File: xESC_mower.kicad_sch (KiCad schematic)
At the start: 48 parts, among them J25 Conn_01x05, J34 Screw_Terminal_01x03, J37 Conn_02x03_Odd_Even, J40 Screw_Terminal_01x02, J43 Conn_01x02, J49 10127820-1022LF, U19 2.54mm 2x2 socket, U22 2.54mm 2x2 socket, U25 2.54mm 2x2 socket, U29 LV2862XDDC, U31 2.54mm 1x6 socket, U34 2.54mm 1x6 socket, U37 2.54mm 1x9 socket, U40 2.54mm 1x5 socket, U9 xESC2

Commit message: Routing progress and vertical USB
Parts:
- J49: Digikey PN (none) -> 609-4876-ND
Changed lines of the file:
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@@
+			)
+		)
+		(property "Digikey PN" "609-4876-ND"
+			(at 240.03 161.29 0)
+			(effects
+				(font
+					(size 1.27 1.27)
+				)
+				(hide yes)
 			)
 		)

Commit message: Incremental routing updates
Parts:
- removed J25: Conn_01x05, Connector_JST:JST_XH_B5B-XH-A_1x05_P2.50mm_Vertical, symbol Connector_Generic:Conn_01x05
- removed J40: Screw_Terminal_01x02, TerminalBlock_Phoenix:TerminalBlock_Phoenix_MKDS-1,5-2-5.08_1x02_P5.08mm_Horizontal, symbol Connector:Screw_Terminal_01x02
- removed J43: Conn_01x02, Connector_AMASS:AMASS_XT30U-M_1x02_P5.0mm_Vertical, symbol Connector_Generic:Conn_01x02

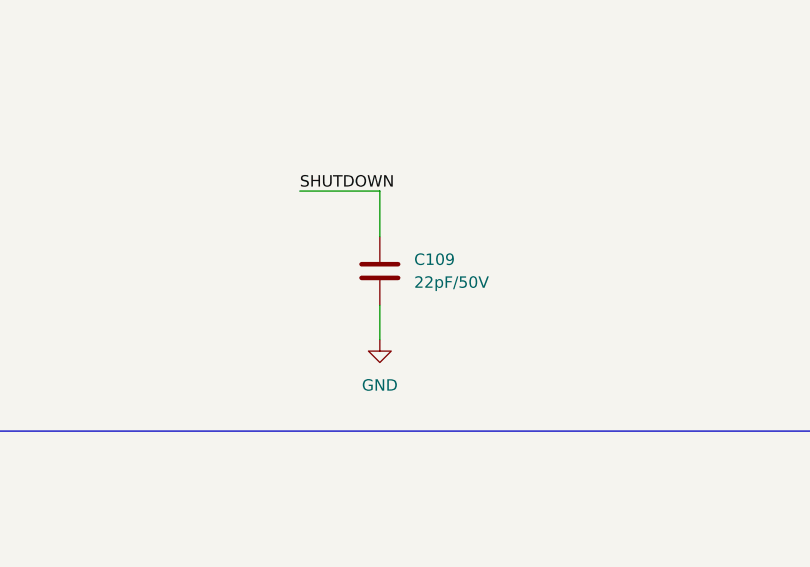
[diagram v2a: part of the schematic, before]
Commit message: Additional routing
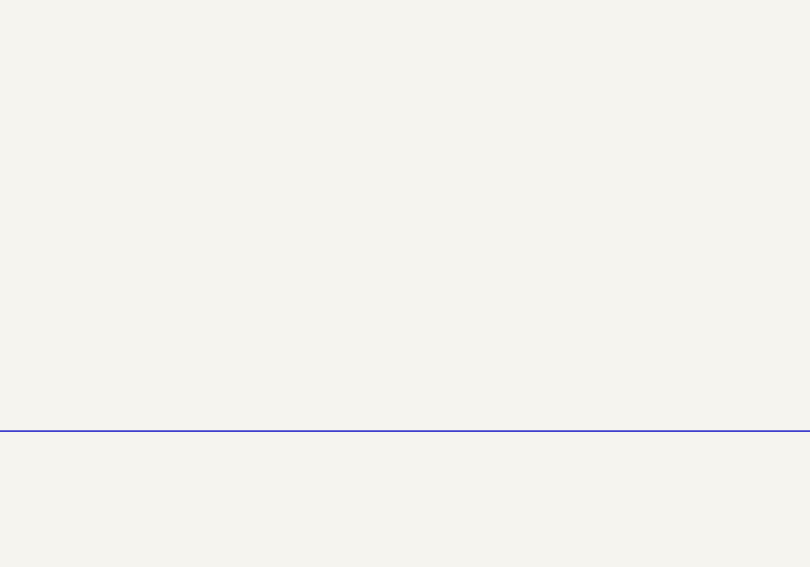
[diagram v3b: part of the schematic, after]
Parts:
- removed C109: 22pF/50V, Capacitor_SMD:C_0603_1608Metric, symbol Device:C

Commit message: Routing progress
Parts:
- D24: now not fitted
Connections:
- net 5V is gone; now on net 5V_Main: C102.1, C103.1, D24.1 (K), D32.2 (A), J37.1 (Pin_1), L6.2, R28.1, U9.5V
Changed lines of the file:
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@@
+	)
+	(junction
+		(at 64.77 60.96)
+		(diameter 0)
+		(color 0 0 0 0)
 	)
 	(junction
@@
 	(junction
 		(at 69.85 100.33)
+		(diameter 0)
+		(color 0 0 0 0)
+	)
+	(junction
+		(at 57.15 60.96)
 		(diameter 0)
 		(color 0 0 0 0)
@@
 	(wire
 		(pts
+			(xy 64.77 57.15) (xy 64.77 60.96)
+		)
+		(stroke
+			(width 0)
+			(type default)
+		)
+	)
+	(wire
+		(pts
 			(xy 124.46 30.48) (xy 118.11 30.48)
 		)
@@
 		(pts
 			(xy 213.36 106.68) (xy 222.25 106.68)
+		)
+		(stroke
+			(width 0)
+			(type default)
+		)
+	)
+	(wire
+		(pts
+			(xy 57.15 60.96) (xy 57.15 57.15)
+		)
+		(stroke
+			(width 0)
+			(type default)
+		)
+	)
+	(wire
+		(pts
+			(xy 57.15 57.15) (xy 64.77 57.15)
 		)
 		(stroke
@@
 		(in_bom yes)
 		(on_board yes)
-		(dnp no)
+		(dnp yes)
 		(fields_autoplaced yes)
 		(property "Reference" "D24"

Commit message: Further routing progress
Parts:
- removed J34: Screw_Terminal_01x03, TerminalBlock_Phoenix:TerminalBlock_Phoenix_MKDS-1,5-3-5.08_1x03_P5.08mm_Horizontal, symbol Connector:Screw_Terminal_01x03
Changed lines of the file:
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@@
 	)
 	(junction
+		(at 222.25 106.68)
+		(diameter 0)
+		(color 0 0 0 0)
+	)
+	(junction
 		(at 44.45 100.33)
 		(diameter 0)
@@
 	)
 	(junction
+		(at 214.63 99.06)
+		(diameter 0)
+		(color 0 0 0 0)
+	)
+	(junction
 		(at 167.64 46.99)
 		(diameter 0)
@@
 	)
 	(junction
-		(at 214.63 99.06)
-		(diameter 0)
-		(color 0 0 0 0)
-	)
-	(junction
 		(at 54.61 107.95)
 		(diameter 0)
@@
 	)
 	(junction
-		(at 184.15 46.99)
+		(at 205.74 102.87)
 		(diameter 0)
 		(color 0 0 0 0)
 	)
 	(junction
-		(at 44.45 107.95)
+		(at 184.15 46.99)
 		(diameter 0)
 		(color 0 0 0 0)
 	)
 	(junction
-		(at 49.53 107.95)
+		(at 44.45 107.95)
 		(diameter 0)
 		(color 0 0 0 0)
 	)
 	(junction
-		(at 205.74 102.87)
+		(at 49.53 107.95)
 		(diameter 0)
 		(color 0 0 0 0)
@@
 	)
 	(junction
-		(at 222.25 106.68)
-		(diameter 0)
-		(color 0 0 0 0)
-	)
-	(junction
 		(at 78.74 36.83)
 		(diameter 0)
@@
 	(wire
 		(pts
+			(xy 214.63 99.06) (xy 226.06 99.06)
+		)
+		(stroke
+			(width 0)
+			(type default)
+		)
+	)
+	(wire
+		(pts
 			(xy 205.74 102.87) (xy 205.74 113.03)
 		)
@@
 	(wire
 		(pts
-			(xy 242.57 99.06) (xy 242.57 100.33)
-		)
-		(stroke
-			(width 0)
-			(type default)
-		)
-	)
-	(wire
-		(pts
 			(xy 284.48 121.92) (xy 306.07 121.92)
 		)
@@
 	(wire
 		(pts
-			(xy 214.63 99.06) (xy 242.57 99.06)
+			(xy 254 121.92) (xy 271.78 121.92)
 		)
 		(stroke
@@
 	(wire
 		(pts
-			(xy 254 121.92) (xy 271.78 121.92)
+			(xy 118.11 41.91) (xy 132.08 41.91)
 		)
 		(stroke
@@
 	(wire
 		(pts
-			(xy 118.11 41.91) (xy 132.08 41.91)
+			(xy 69.85 107.95) (xy 74.93 107.95)
 		)
 		(stroke
@@
 	(wire
 		(pts
-			(xy 69.85 107.95) (xy 74.93 107.95)
+			(xy 195.58 99.06) (xy 214.63 99.06)
 		)
 		(stroke
@@
 	(wire
 		(pts
-			(xy 195.58 99.06) (xy 214.63 99.06)
+			(xy 132.08 104.14) (xy 142.24 104.14)
 		)
 		(stroke
@@
 	(wire
 		(pts
-			(xy 132.08 104.14) (xy 142.24 104.14)
+			(xy 222.25 106.68) (xy 226.06 106.68)
 		)
 		(stroke
@@
 	(wire
 		(pts
-			(xy 222.25 106.68) (xy 242.57 106.68)
-		)
-		(stroke
-			(width 0)
-			(type default)
-		)
-	)
-	(wire
-		(pts
 			(xy 29.21 100.33) (xy 39.37 100.33)
 		)
@@
 	(wire
 		(pts
-			(xy 242.57 106.68) (xy 242.57 105.41)
-		)
-		(stroke
-			(width 0)
-			(type default)
-		)
-	)
-	(wire
-		(pts
 			(xy 74.93 100.33) (xy 90.17 100.33)
 		)
@@
 	(wire
 		(pts
-			(xy 57.15 57.15) (xy 64.77 57.15)
+			(xy 205.74 102.87) (xy 226.06 102.87)
 		)
 		(stroke
@@
 	(wire
 		(pts
-			(xy 193.04 121.92) (xy 243.84 121.92)
+			(xy 57.15 57.15) (xy 64.77 57.15)
 		)
 		(stroke
@@
 	(wire
 		(pts
-			(xy 222.25 149.86) (xy 227.33 149.86)
+			(xy 193.04 121.92) (xy 243.84 121.92)
 		)
 		(stroke
@@
 	(wire
 		(pts
-			(xy 205.74 102.87) (xy 242.57 102.87)
+			(xy 222.25 149.86) (xy 227.33 149.86)
 		)
 		(stroke
@@
 					(unit 1)
 				)
-			)
-		)
-	)
-	(symbol
-		(lib_id "Connector:Screw_Terminal_01x03")
-		(at 247.65 102.87 0)
-		(unit 1)
-		(exclude_from_sim no)
-		(in_bom yes)
-		(on_board yes)
-		(dnp no)
-		(fields_autoplaced yes)
-		(property "Reference" "J34"
-			(at 250.19 101.5999 0)
-			(effects
-				(font
-					(size 1.27 1.27)
-				)
-				(justify left)
-			)
-		)
-		(property "Value" "Screw_Terminal_01x03"
-			(at 250.19 104.1399 0)
-			(effects
-				(font
-					(size 1.27 1.27)
-				)
-				(justify left)
-			)
-		)
-		(property "Footprint" "TerminalBlock_Phoenix:TerminalBlock_Phoenix_MKDS-1,5-3-5.08_1x03_P5.08mm_Horizontal"
-			(at 247.65 102.87 0)
-			(effects
-				(font
-					(size 1.27 1.27)
-				)
-				(hide yes)
-			)
-		)
-		(property "Datasheet" "~"
-			(at 247.65 102.87 0)
-			(effects
-				(font
-					(size 1.27 1.27)
-				)
-				(hide yes)
-			)
-		)
-		(property "Description" "Generic screw terminal, single row, 01x03, script generated (kicad-library-utils/schlib/autogen/connector/)"
-			(at 247.65 102.87 0)
-			(effects
-				(font
-					(size 1.27 1.27)
-				)
-				(hide yes)
-			)
-		)
-		(property "Field4" ""
-			(at 247.65 102.87 0)
-			(effects
-				(font
-					(size 1.27 1.27)
-				)
-				(hide yes)
-			)
-		)
-		(property "Field5" ""
-			(at 247.65 102.87 0)
-			(effects
-				(font
-					(size 1.27 1.27)
-				)
-				(hide yes)
-			)
-		)
-		(property "Field6" ""
-			(at 247.65 102.87 0)
-			(effects
-				(font
-					(size 1.27 1.27)
-				)
-				(hide yes)
-			)
-		)
-		(property "Field7" ""
-			(at 247.65 102.87 0)
-			(effects
-				(font
-					(size 1.27 1.27)
-				)
-				(hide yes)
-			)
-		)
-		(property "JLC" "C557666"
-			(at 247.65 102.87 0)
-			(effects
-				(font
-					(size 1.27 1.27)
-				)
-				(hide yes)
-			)
-		)
-		(property "Part Description" ""
-			(at 247.65 102.87 0)
-			(effects
-				(font
-					(size 1.27 1.27)
-				)
-				(hide yes)
-			)
-		)
-		(property "Height" ""
-			(at 247.65 102.87 0)
-			(effects
-				(font
-					(size 1.27 1.27)
-				)
-				(hide yes)
-			)
-		)
-		(property "Manufacturer_Name" ""
-			(at 247.65 102.87 0)
-			(effects
-				(font
-					(size 1.27 1.27)
-				)
-				(hide yes)
-			)
-		)
-		(property "Manufacturer_Part_Number" ""
-			(at 247.65 102.87 0)
-			(effects
-				(font
-					(size 1.27 1.27)
-				)
-				(hide yes)
-			)
-		)
-		(property "Mouser Part Number" ""
-			(at 247.65 102.87 0)
-			(effects
-				(font
-					(size 1.27 1.27)
-				)
-				(hide yes)
-			)
-		)
-		(property "Mouser Price/Stock" ""
-			(at 247.65 102.87 0)
-			(effects
-				(font
-					(size 1.27 1.27)
-				)
-				(hide yes)
-			)
-		)
-		(pin "3"
-		)
-		(pin "2"
-		)
-		(pin "1"
-		)
-		(instances
-			(project "hw-openmower-universal"
-				(path "/e12e8a63-1d1b-4736-9aba-a87a258b2b11/35c1a146-5cd7-4cc8-a12d-17de73f02598"
-					(reference "J34")
-					(unit 1)
-				)

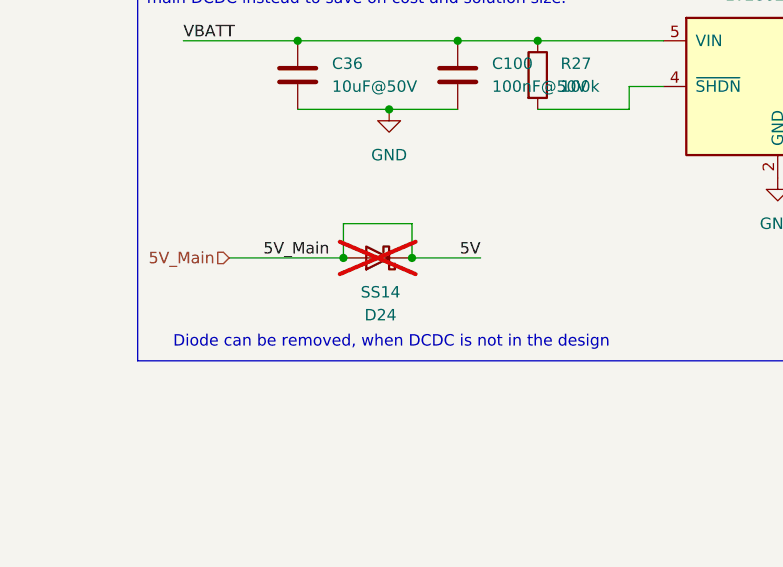
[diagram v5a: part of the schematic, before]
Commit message: Review ready layout
DRC mostly clean.  Need to add GND via stitching and GND return vias yet, and general review
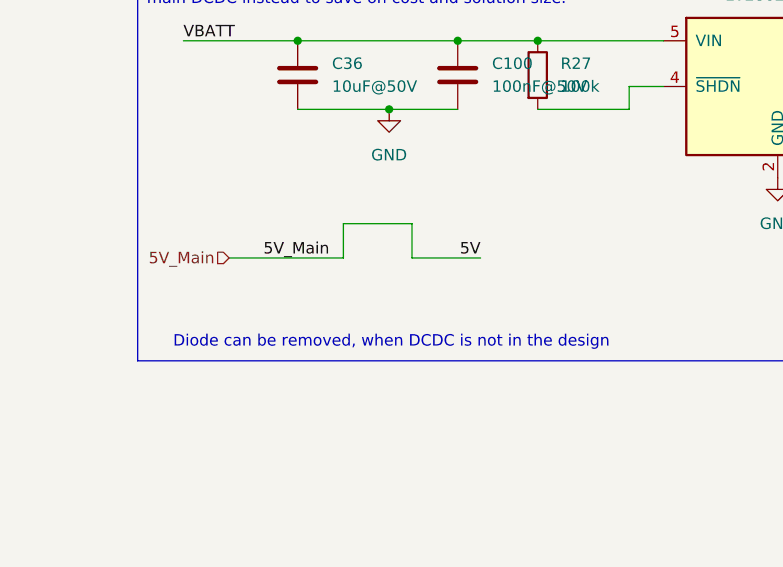
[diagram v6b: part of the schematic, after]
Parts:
- removed D24: SS14, Diode_SMD:D_SMA, symbol Diode:SS14
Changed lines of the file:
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@@
-	)
-	(junction
-		(at 64.77 60.96)
-		(diameter 0)
-		(color 0 0 0 0)
 	)
 	(junction
@@
 	(junction
 		(at 69.85 100.33)
-		(diameter 0)
-		(color 0 0 0 0)
-	)
-	(junction
-		(at 57.15 60.96)
 		(diameter 0)
 		(color 0 0 0 0)
@@
 					(unit 1)
 				)
-			)
-		)
-	)
-	(symbol
-		(lib_id "Diode:SS14")
-		(at 60.96 60.96 180)
-		(unit 1)
-		(exclude_from_sim no)
-		(in_bom yes)
-		(on_board yes)
-		(dnp yes)
-		(fields_autoplaced yes)
-		(property "Reference" "D24"
-			(at 61.2775 67.31 0)
-			(effects
-				(font
-					(size 1.27 1.27)
-				)
-			)
-		)
-		(property "Value" "SS14"
-			(at 61.2775 64.77 0)
-			(effects
-				(font
-					(size 1.27 1.27)
-				)
-			)
-		)
-		(property "Footprint" "Diode_SMD:D_SMA"
-			(at 60.96 56.515 0)
-			(effects
-				(font
-					(size 1.27 1.27)
-				)
-				(hide yes)
-			)
-		)
-		(property "Datasheet" "https://www.vishay.com/docs/88746/ss12.pdf"
-			(at 60.96 60.96 0)
-			(effects
-				(font
-					(size 1.27 1.27)
-				)
-				(hide yes)
-			)
-		)
-		(property "Description" "40V 1A Schottky Diode, SMA"
-			(at 60.96 60.96 0)
-			(effects
-				(font
-					(size 1.27 1.27)
-				)
-				(hide yes)
-			)
-		)
-		(property "Field4" ""
-			(at 60.96 60.96 0)
-			(effects
-				(font
-					(size 1.27 1.27)
-				)
-				(hide yes)
-			)
-		)
-		(property "Field5" ""
-			(at 60.96 60.96 0)
-			(effects
-				(font
-					(size 1.27 1.27)
-				)
-				(hide yes)
-			)
-		)
-		(property "Field6" ""
-			(at 60.96 60.96 0)
-			(effects
-				(font
-					(size 1.27 1.27)
-				)
-				(hide yes)
-			)
-		)
-		(property "Field7" ""
-			(at 60.96 60.96 0)
-			(effects
-				(font
-					(size 1.27 1.27)
-				)
-				(hide yes)
-			)
-		)
-		(property "JLC" "C2480"
-			(at 60.96 60.96 0)
-			(effects
-				(font
-					(size 1.27 1.27)
-				)
-				(hide yes)
-			)
-		)
-		(property "Part Description" ""
-			(at 60.96 60.96 0)
-			(effects
-				(font
-					(size 1.27 1.27)
-				)
-				(hide yes)
-			)
-		)
-		(property "Height" ""
-			(at 60.96 60.96 0)
-			(effects
-				(font
-					(size 1.27 1.27)
-				)
-				(hide yes)
-			)
-		)
-		(property "Manufacturer_Name" ""
-			(at 60.96 60.96 0)
-			(effects
-				(font
-					(size 1.27 1.27)
-				)
-				(hide yes)
-			)
-		)
-		(property "Manufacturer_Part_Number" ""
-			(at 60.96 60.96 0)
-			(effects
-				(font
-					(size 1.27 1.27)
-				)
-				(hide yes)
-			)
-		)
-		(property "Mouser Part Number" ""
-			(at 60.96 60.96 0)
-			(effects
-				(font
-					(size 1.27 1.27)
-				)
-				(hide yes)
-			)
-		)
-		(property "Mouser Price/Stock" ""
-			(at 60.96 60.96 0)
-			(effects
-				(font
-					(size 1.27 1.27)
-				)
-				(hide yes)
-			)
-		)
-		(pin "2"
-		)
-		(pin "1"
-		)
-		(instances
-			(project "hw-openmower-universal"
-				(path "/e12e8a63-1d1b-4736-9aba-a87a258b2b11/35c1a146-5cd7-4cc8-a12d-17de73f02598"
-					(reference "D24")
-					(unit 1)
-				)
